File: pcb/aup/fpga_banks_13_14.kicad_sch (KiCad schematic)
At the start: 1 part, among them U1 XC7A50T-2FGG484C

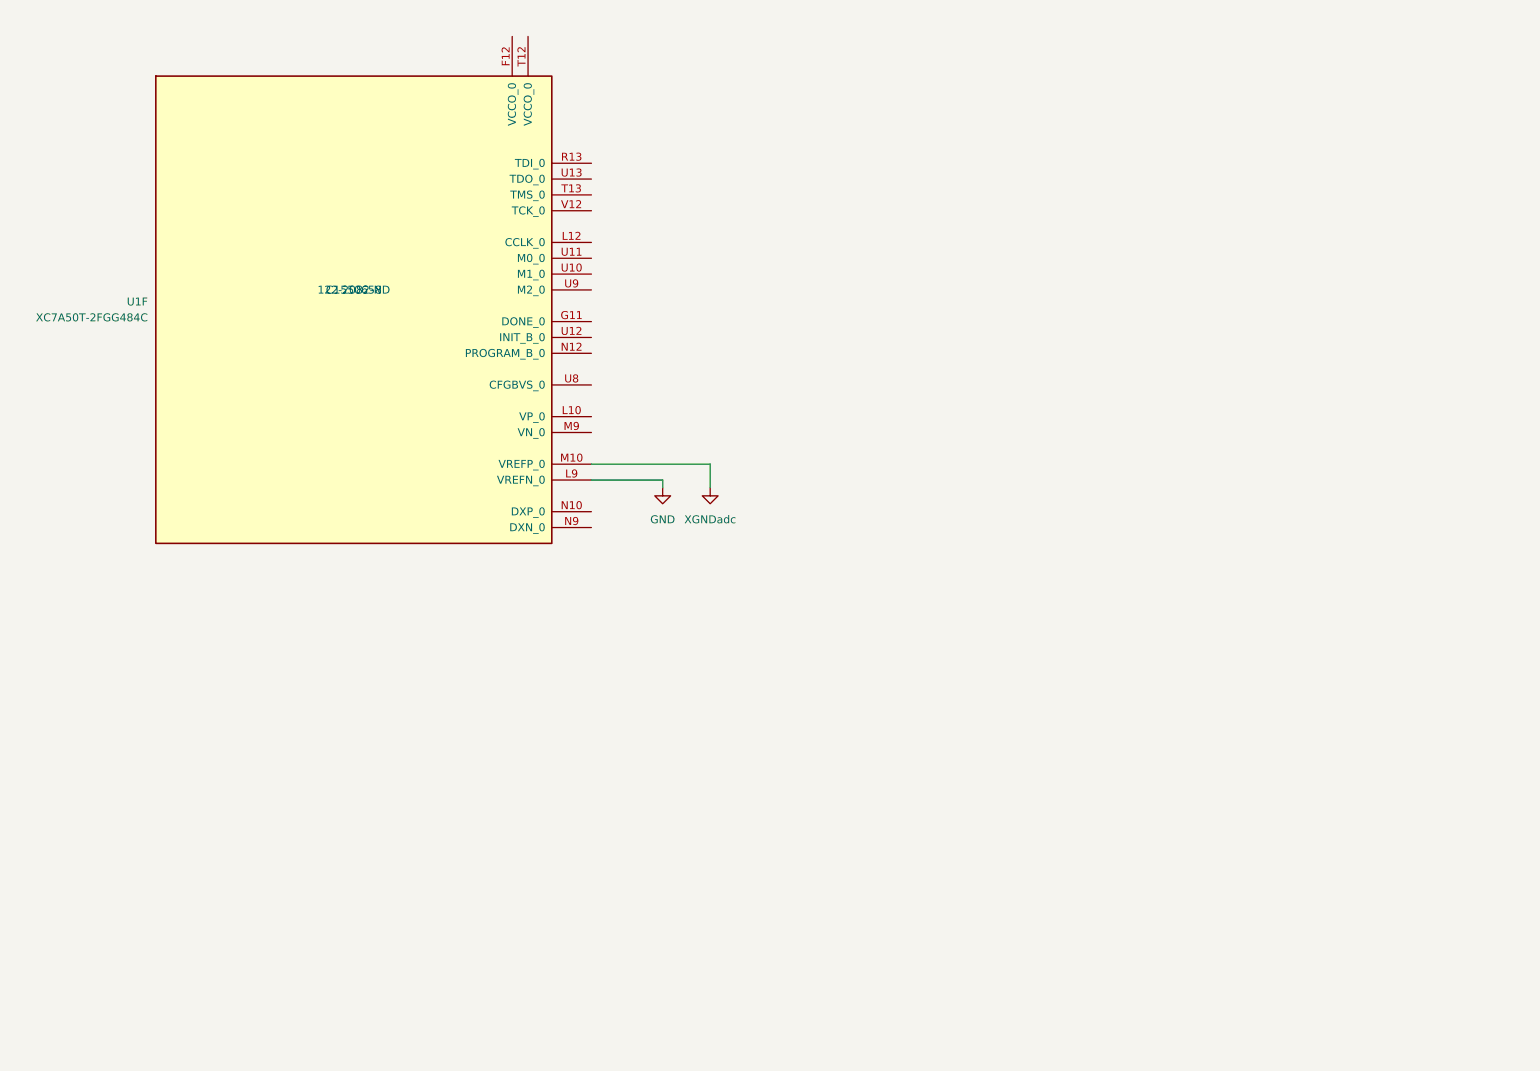
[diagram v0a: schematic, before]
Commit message: Add hierarchical sheets for banks and add caps.
There are some stale sheets in this commit, but I don't want to delete
an active one accidentally. Save them all for now, and then go back and
clean them up.
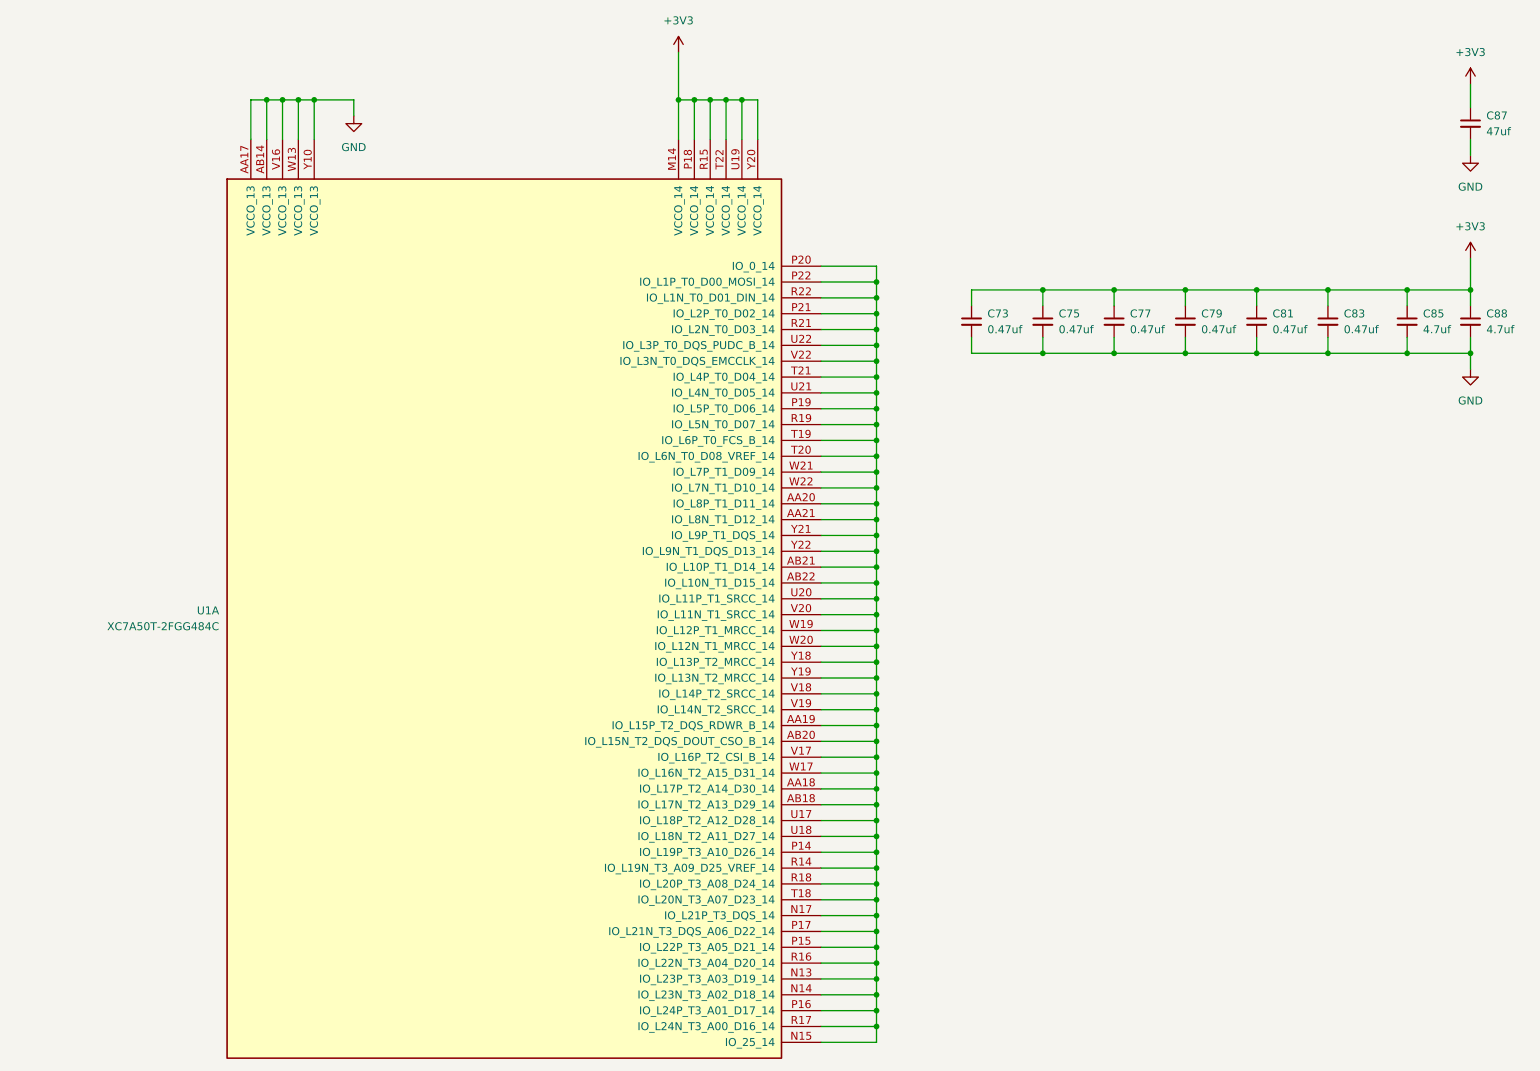
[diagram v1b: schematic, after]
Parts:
- removed U1: XC7A50T-2FGG484C, !Xilinx:Xilinx_FGG484, symbol !Xilinx:XC7A50T-FGG484
- added C73, C75, C77, C79, C81, C83: 0.47uf, Capacitor_SMD:C_0402_1005Metric, symbol !Misc:C_0.47uf_0402
- added C85, C88: 4.7uf, Capacitor_SMD:C_0805_2012Metric, symbol !Misc:C_4.7uf_0805
- added C87: 47uf, Capacitor_SMD:C_1206_3216Metric, symbol !Misc:C_47uf_1206
- added U1: XC7A50T-2FGG484C, !Xilinx:Xilinx_FGG484, symbol !Xilinx:XC7A50T-FGG484
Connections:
- net GND: now also C73.2, C75.2, C77.2, C79.2, C81.2, C83.2, C85.2, C87.2, C88.2, U1.AA17 (VCCO_13), U1.AB14 (VCCO_13), U1.V16 (VCCO_13), U1.W13 (VCCO_13), U1.Y10 (VCCO_13)
- new net: U1.AA18 (IO_L17P_T2_A14_D30_14), U1.AA19 (IO_L15P_T2_DQS_RDWR_B_14), U1.AA20 (IO_L8P_T1_D11_14), U1.AA21 (IO_L8N_T1_D12_14), U1.AB18 (IO_L17N_T2_A13_D29_14), U1.AB20 (IO_L15N_T2_DQS_DOUT_CSO_B_14), U1.AB21 (IO_L10P_T1_D14_14), U1.AB22 (IO_L10N_T1_D15_14), U1.N13 (IO_L23P_T3_A03_D19_14), U1.N14 (IO_L23N_T3_A02_D18_14), U1.N15 (IO_25_14), U1.N17 (IO_L21P_T3_DQS_14), U1.P14 (IO_L19P_T3_A10_D26_14), U1.P15 (IO_L22P_T3_A05_D21_14), U1.P16 (IO_L24P_T3_A01_D17_14), U1.P17 (IO_L21N_T3_DQS_A06_D22_14), U1.P19 (IO_L5P_T0_D06_14), U1.P20 (IO_0_14), U1.P21 (IO_L2P_T0_D02_14), U1.P22 (IO_L1P_T0_D00_MOSI_14), U1.R14 (IO_L19N_T3_A09_D25_VREF_14), U1.R16 (IO_L22N_T3_A04_D20_14), U1.R17 (IO_L24N_T3_A00_D16_14), U1.R18 (IO_L20P_T3_A08_D24_14), U1.R19 (IO_L5N_T0_D07_14), U1.R21 (IO_L2N_T0_D03_14), U1.R22 (IO_L1N_T0_D01_DIN_14), U1.T18 (IO_L20N_T3_A07_D23_14), U1.T19 (IO_L6P_T0_FCS_B_14), U1.T20 (IO_L6N_T0_D08_VREF_14), U1.T21 (IO_L4P_T0_D04_14), U1.U17 (IO_L18P_T2_A12_D28_14), U1.U18 (IO_L18N_T2_A11_D27_14), U1.U20 (IO_L11P_T1_SRCC_14), U1.U21 (IO_L4N_T0_D05_14), U1.U22 (IO_L3P_T0_DQS_PUDC_B_14), U1.V17 (IO_L16P_T2_CSI_B_14), U1.V18 (IO_L14P_T2_SRCC_14), U1.V19 (IO_L14N_T2_SRCC_14), U1.V20 (IO_L11N_T1_SRCC_14), U1.V22 (IO_L3N_T0_DQS_EMCCLK_14), U1.W17 (IO_L16N_T2_A15_D31_14), U1.W19 (IO_L12P_T1_MRCC_14), U1.W20 (IO_L12N_T1_MRCC_14), U1.W21 (IO_L7P_T1_D09_14), U1.W22 (IO_L7N_T1_D10_14), U1.Y18 (IO_L13P_T2_MRCC_14), U1.Y19 (IO_L13N_T2_MRCC_14), U1.Y21 (IO_L9P_T1_DQS_14), U1.Y22 (IO_L9N_T1_DQS_D13_14)
- new net +3V3: C73.1, C75.1, C77.1, C79.1, C81.1, C83.1, C85.1, C87.1, C88.1, U1.M14 (VCCO_14), U1.P18 (VCCO_14), U1.R15 (VCCO_14), U1.T22 (VCCO_14), U1.U19 (VCCO_14), U1.Y20 (VCCO_14)

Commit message: Switch 0.47uf caps under bga to 0201
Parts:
- C73, C75, C77, C79, C81, C83: footprint Capacitor_SMD:C_0402_1005Metric -> Capacitor_SMD:C_0201_0603Metric; symbol !Misc:C_0.47uf_0402 -> !Misc:C_0.47uf_0201; Digi-Key Part Number 1276-1173-1-ND -> 1276-1337-1-ND; LCSC Part # C1779 -> C318543
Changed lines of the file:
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@@
 	)
 	(symbol
-		(lib_id "!Misc:C_0.47uf_0402")
+		(lib_id "!Misc:C_0.47uf_0201")
 		(at 227.33 68.58 0)
 		(unit 1)
@@
 			)
 		)
-		(property "Footprint" "Capacitor_SMD:C_0402_1005Metric"
+		(property "Footprint" "Capacitor_SMD:C_0201_0603Metric"
 			(at 227.33 68.58 0)
 			(effects
@@
 			)
 		)
-		(property "Description" "Unpolarized capacitor 0.47uf 0402"
+		(property "Description" "Unpolarized capacitor 0.47uf 0201"
 			(at 227.33 68.58 0)
 			(effects
@@
 			)
 		)
-		(property "LCSC Part #" "C1779"
+		(property "LCSC Part #" "C318543"
 			(at 227.33 68.58 0)
 			(effects
@@
 			)
 		)
-		(property "Digi-Key Part Number" "1276-1173-1-ND"
+		(property "Digi-Key Part Number" "1276-1337-1-ND"
 			(at 227.33 68.58 0)
 			(effects
@@
 	)
 	(symbol
-		(lib_id "!Misc:C_0.47uf_0402")
+		(lib_id "!Misc:C_0.47uf_0201")
 		(at 170.18 68.58 0)
 		(unit 1)
@@
 			)
 		)
-		(property "Footprint" "Capacitor_SMD:C_0402_1005Metric"
+		(property "Footprint" "Capacitor_SMD:C_0201_0603Metric"
 			(at 170.18 68.58 0)
 			(effects
@@
 			)
 		)
-		(property "Description" "Unpolarized capacitor 0.47uf 0402"
+		(property "Description" "Unpolarized capacitor 0.47uf 0201"
 			(at 170.18 68.58 0)
 			(effects
@@
 			)
 		)
-		(property "LCSC Part #" "C1779"
+		(property "LCSC Part #" "C318543"
 			(at 170.18 68.58 0)
 			(effects
@@
 			)
 		)
-		(property "Digi-Key Part Number" "1276-1173-1-ND"
+		(property "Digi-Key Part Number" "1276-1337-1-ND"
 			(at 170.18 68.58 0)
 			(effects
@@
 	)
 	(symbol
-		(lib_id "!Misc:C_0.47uf_0402")
+		(lib_id "!Misc:C_0.47uf_0201")
 		(at 181.61 68.58 0)
 		(unit 1)
@@
 			)
 		)
-		(property "Footprint" "Capacitor_SMD:C_0402_1005Metric"
+		(property "Footprint" "Capacitor_SMD:C_0201_0603Metric"
 			(at 181.61 68.58 0)
 			(effects
@@
 			)
 		)
-		(property "Description" "Unpolarized capacitor 0.47uf 0402"
+		(property "Description" "Unpolarized capacitor 0.47uf 0201"
 			(at 181.61 68.58 0)
 			(effects
@@
 			)
 		)
-		(property "LCSC Part #" "C1779"
+		(property "LCSC Part #" "C318543"
 			(at 181.61 68.58 0)
 			(effects
@@
 			)
 		)
-		(property "Digi-Key Part Number" "1276-1173-1-ND"
+		(property "Digi-Key Part Number" "1276-1337-1-ND"
 			(at 181.61 68.58 0)
 			(effects
@@
 	)
 	(symbol
-		(lib_id "!Misc:C_0.47uf_0402")
+		(lib_id "!Misc:C_0.47uf_0201")
 		(at 215.9 68.58 0)
 		(unit 1)
@@
 			)
 		)
-		(property "Footprint" "Capacitor_SMD:C_0402_1005Metric"
+		(property "Footprint" "Capacitor_SMD:C_0201_0603Metric"
 			(at 215.9 68.58 0)
 			(effects
@@
 			)
 		)
-		(property "Description" "Unpolarized capacitor 0.47uf 0402"
+		(property "Description" "Unpolarized capacitor 0.47uf 0201"
 			(at 215.9 68.58 0)
 			(effects
@@
 			)
 		)
-		(property "LCSC Part #" "C1779"
+		(property "LCSC Part #" "C318543"
 			(at 215.9 68.58 0)
 			(effects
@@
 			)
 		)
-		(property "Digi-Key Part Number" "1276-1173-1-ND"
+		(property "Digi-Key Part Number" "1276-1337-1-ND"
 			(at 215.9 68.58 0)
 			(effects
@@
 	)
 	(symbol
-		(lib_id "!Misc:C_0.47uf_0402")
+		(lib_id "!Misc:C_0.47uf_0201")
 		(at 204.47 68.58 0)
 		(unit 1)
@@
 			)
 		)
-		(property "Footprint" "Capacitor_SMD:C_0402_1005Metric"
+		(property "Footprint" "Capacitor_SMD:C_0201_0603Metric"
 			(at 204.47 68.58 0)
 			(effects
@@
 			)
 		)
-		(property "Description" "Unpolarized capacitor 0.47uf 0402"
+		(property "Description" "Unpolarized capacitor 0.47uf 0201"
 			(at 204.47 68.58 0)
 			(effects
@@
 			)
 		)
-		(property "LCSC Part #" "C1779"
+		(property "LCSC Part #" "C318543"
 			(at 204.47 68.58 0)
 			(effects
@@
 			)
 		)
-		(property "Digi-Key Part Number" "1276-1173-1-ND"
+		(property "Digi-Key Part Number" "1276-1337-1-ND"
 			(at 204.47 68.58 0)
 			(effects
@@
 	)
 	(symbol
-		(lib_id "!Misc:C_0.47uf_0402")
+		(lib_id "!Misc:C_0.47uf_0201")
 		(at 193.04 68.58 0)
 		(unit 1)
@@
 			)
 		)
-		(property "Footprint" "Capacitor_SMD:C_0402_1005Metric"
+		(property "Footprint" "Capacitor_SMD:C_0201_0603Metric"
 			(at 193.04 68.58 0)
 			(effects
@@
 			)
 		)
-		(property "Description" "Unpolarized capacitor 0.47uf 0402"
+		(property "Description" "Unpolarized capacitor 0.47uf 0201"
 			(at 193.04 68.58 0)
 			(effects
@@
 			)
 		)
-		(property "LCSC Part #" "C1779"
+		(property "LCSC Part #" "C318543"
 			(at 193.04 68.58 0)
 			(effects
@@
 			)
 		)
-		(property "Digi-Key Part Number" "1276-1173-1-ND"
+		(property "Digi-Key Part Number" "1276-1337-1-ND"
 			(at 193.04 68.58 0)
 			(effects
